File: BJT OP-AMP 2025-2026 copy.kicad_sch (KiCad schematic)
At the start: 35 parts, among them J1 Conn_01x05, Q1 2N3904TA, Q2 2N3904TA, Q3 MMDT3904, Q4 MMDT3906, Q5 2N3904TA, Q8 2N3906BU, Q9 2N3904TA

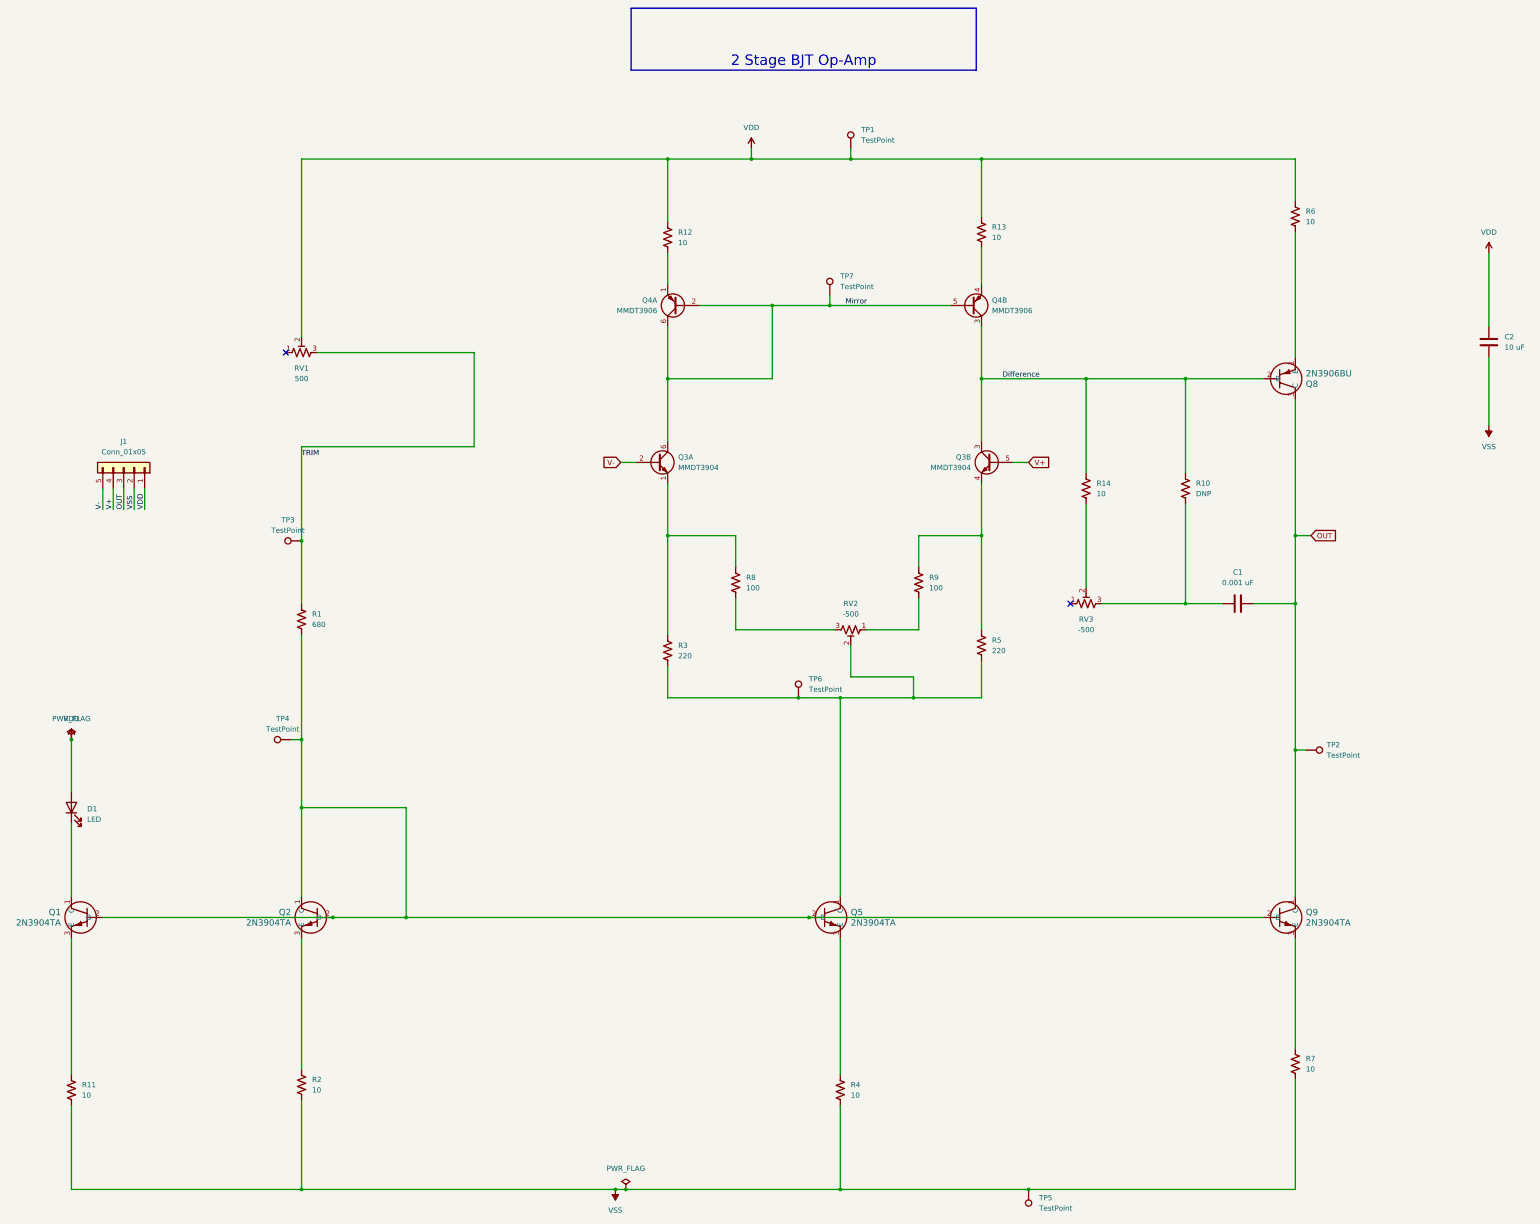
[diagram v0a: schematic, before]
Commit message: Finished Board & Updated Schematic
This is the finished board on KiCad with downloaded footprints from Digikey for 2N3904TA & 2N3906BU. Board ran with DRC works fine but footprint clearance errors because of downloaded parts from Digikey. Also, updated schematic used for running LTSpice.
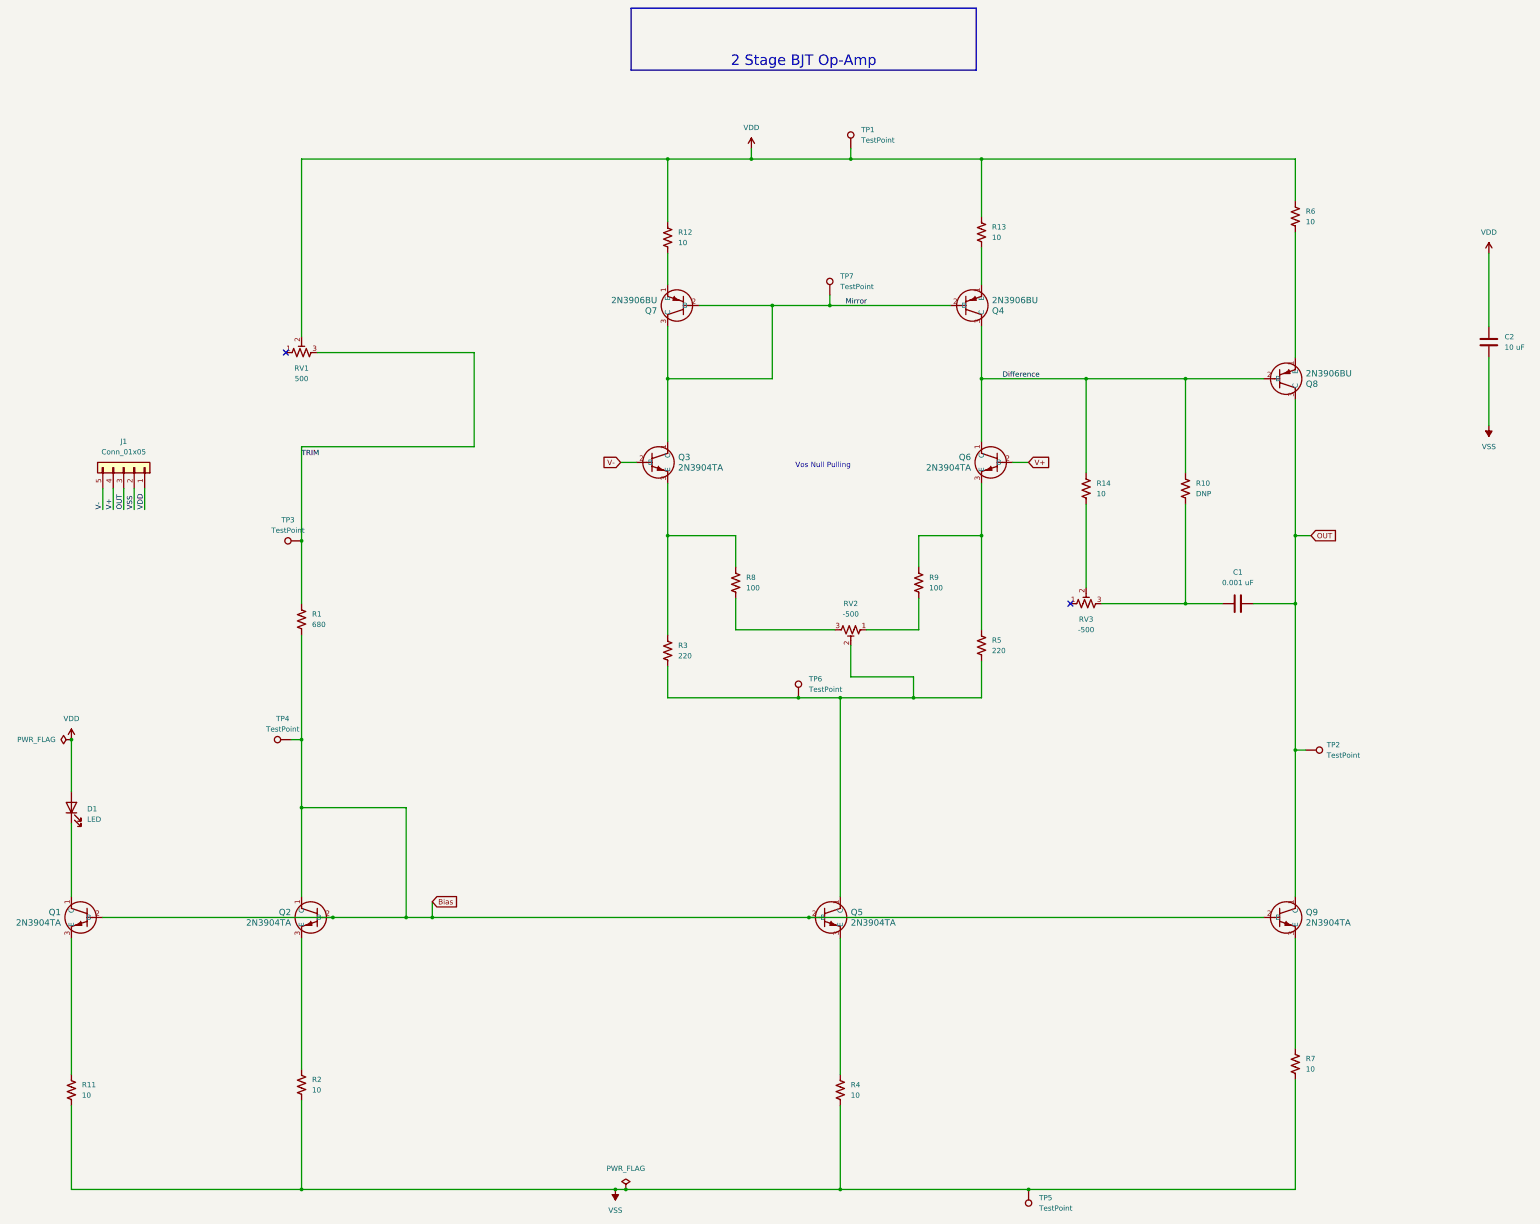
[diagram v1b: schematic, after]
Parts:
- removed Q3: MMDT3904, Package_TO_SOT_SMD:SOT-363_SC-70-6, symbol Transistor_BJT:MMDT3904
- removed Q4: MMDT3906, Package_TO_SOT_SMD:SOT-363_SC-70-6, symbol Transistor_BJT:MMDT3906
- added Q3, Q6: 2N3904TA, Footprints AAMU Capstone:2N3904TA_ONS, symbol 2025-09-01_17-38-56:2N3904TA
- added Q4, Q7: 2N3906BU, Footprints AAMU Capstone:2N3906BU_ONS, symbol 2025-09-01_17-32-00:2N3906BU
- D1: footprint (none) -> LED_SMD:LED_0603_1608Metric_Pad1.05x0.95mm_HandSolder
- J1: footprint Connector_PinHeader_2.54mm:PinHeader_1x05_P2.54mm_Vertical -> Connector_PinHeader_2.54mm:PinHeader_1x05_P2.54mm_Horizontal
- Q1, Q2, Q5, Q9: footprint Footprints AAMU Capstone:TNPN_TO-92_ONS -> Footprints AAMU Capstone:2N3904TA_ONS
- RV1, RV2, RV3: footprint (none) -> Footprints AAMU Capstone:TRIM_3306F-1-253
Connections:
- net Difference: now also Q4.3 (C), Q6.1 (C)
- net Mirror: now also Q3.1 (C), Q4.2 (B), Q7.2 (B), Q7.3 (C)
- net V+: now also Q6.2 (B)
- net V-: now also Q3.2 (B)
- net at R3.1, R8.1: now also Q3.3 (E)
- net Bias: now reaches Q1.2 (B), Q2.1 (C), Q2.2 (B), Q5.2 (B), Q9.2 (B), R1.2, TP4.1
- net at R12.2: now also Q7.1 (E)
- net at R5.1, R9.1: now also Q6.3 (E)
- net at R13.2: now also Q4.1 (E)
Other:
- note added: "Vos Null Pulling"
